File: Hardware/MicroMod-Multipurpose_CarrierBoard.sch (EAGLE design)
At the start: 85 parts, among them J11 microSD, J12 SPI, J14 I2C, J16 General GPIO, J17 I2C1, J3 JTAG, J5 UART, J6 MICROMOD-2222-C, J8 Dedicated, Q2 600mA/40V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

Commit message: Connect buzzer via MicroMod PWM0 via normally-connected trace
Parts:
- added BUZZER: JUMPER-COMBO_2_NC_TRACE, SparkFun-Jumpers:JUMPER-COMBO_2_NC_TRACE
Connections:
- net BUZZER: now also BUZZER.1
- net PWM0: now also BUZZER.2
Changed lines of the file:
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@@
 <part name="J17" library="SparkFun-Connectors" deviceset="I2C_STANDARD" device="_NO_SILK" value="I2C1"/>
 <part name="GND37" library="SparkFun-PowerSymbols" deviceset="GND" device=""/>
+<part name="BUZZER" library="SparkFun-Jumpers" deviceset="JUMPER-COMBO_2_NC_TRACE" device="" value=""/>
 </parts>
 <sheets>
@@
 <attribute name="VALUE" x="99.06" y="4.826" size="1.778" layer="96" align="top-center"/>
 </instance>
+<instance part="BUZZER" gate="JP1" x="386.08" y="134.62" smashed="yes" rot="R90">
+<attribute name="NAME" x="384.048" y="128.27" size="1.778" layer="95" font="vector" rot="R90"/>
+<attribute name="VALUE" x="388.62" y="132.08" size="1.778" layer="96" font="vector" rot="R90" align="top-left"/>
+</instance>
 </instances>
 <busses>
@@
 <label x="33.02" y="78.74" size="1.27" layer="95" rot="R180" xref="yes"/>
 </segment>
+<segment>
+<pinref part="BUZZER" gate="JP1" pin="2"/>
+<wire x1="386.08" y1="139.7" x2="386.08" y2="142.24" width="0.1524" layer="91"/>
+<wire x1="386.08" y1="142.24" x2="388.62" y2="142.24" width="0.1524" layer="91"/>
+<label x="388.62" y="142.24" size="1.27" layer="95" xref="yes"/>
+</segment>
 </net>
 <net name="PWM1" class="0">
@@
 <label x="78.74" y="38.1" size="1.27" layer="95" rot="R180" xref="yes"/>
 <pinref part="J12" gate="G$1" pin="5"/>
-</segment>
-</net>
-<net name="BUZZER" class="0">
-<segment>
-<pinref part="R17" gate="G$1" pin="1"/>
-<wire x1="396.24" y1="121.92" x2="393.7" y2="121.92" width="0.1524" layer="91"/>
-<label x="393.7" y="121.92" size="1.27" layer="95" rot="R180" xref="yes"/>
 </segment>
 </net>
@@
 </segment>
 </net>
+<net name="BUZZER" class="0">
+<segment>
+<pinref part="BUZZER" gate="JP1" pin="1"/>
+<wire x1="386.08" y1="129.54" x2="386.08" y2="127" width="0.1524" layer="91"/>
+<pinref part="R17" gate="G$1" pin="1"/>
+<wire x1="386.08" y1="127" x2="386.08" y2="121.92" width="0.1524" layer="91"/>
+<wire x1="386.08" y1="121.92" x2="396.24" y2="121.92" width="0.1524" layer="91"/>
+<wire x1="386.08" y1="127" x2="388.62" y2="127" width="0.1524" layer="91"/>
+<junction x="386.08" y="127"/>
+<label x="388.62" y="127" size="1.27" layer="95" xref="yes"/>
+</segment>
+</net>

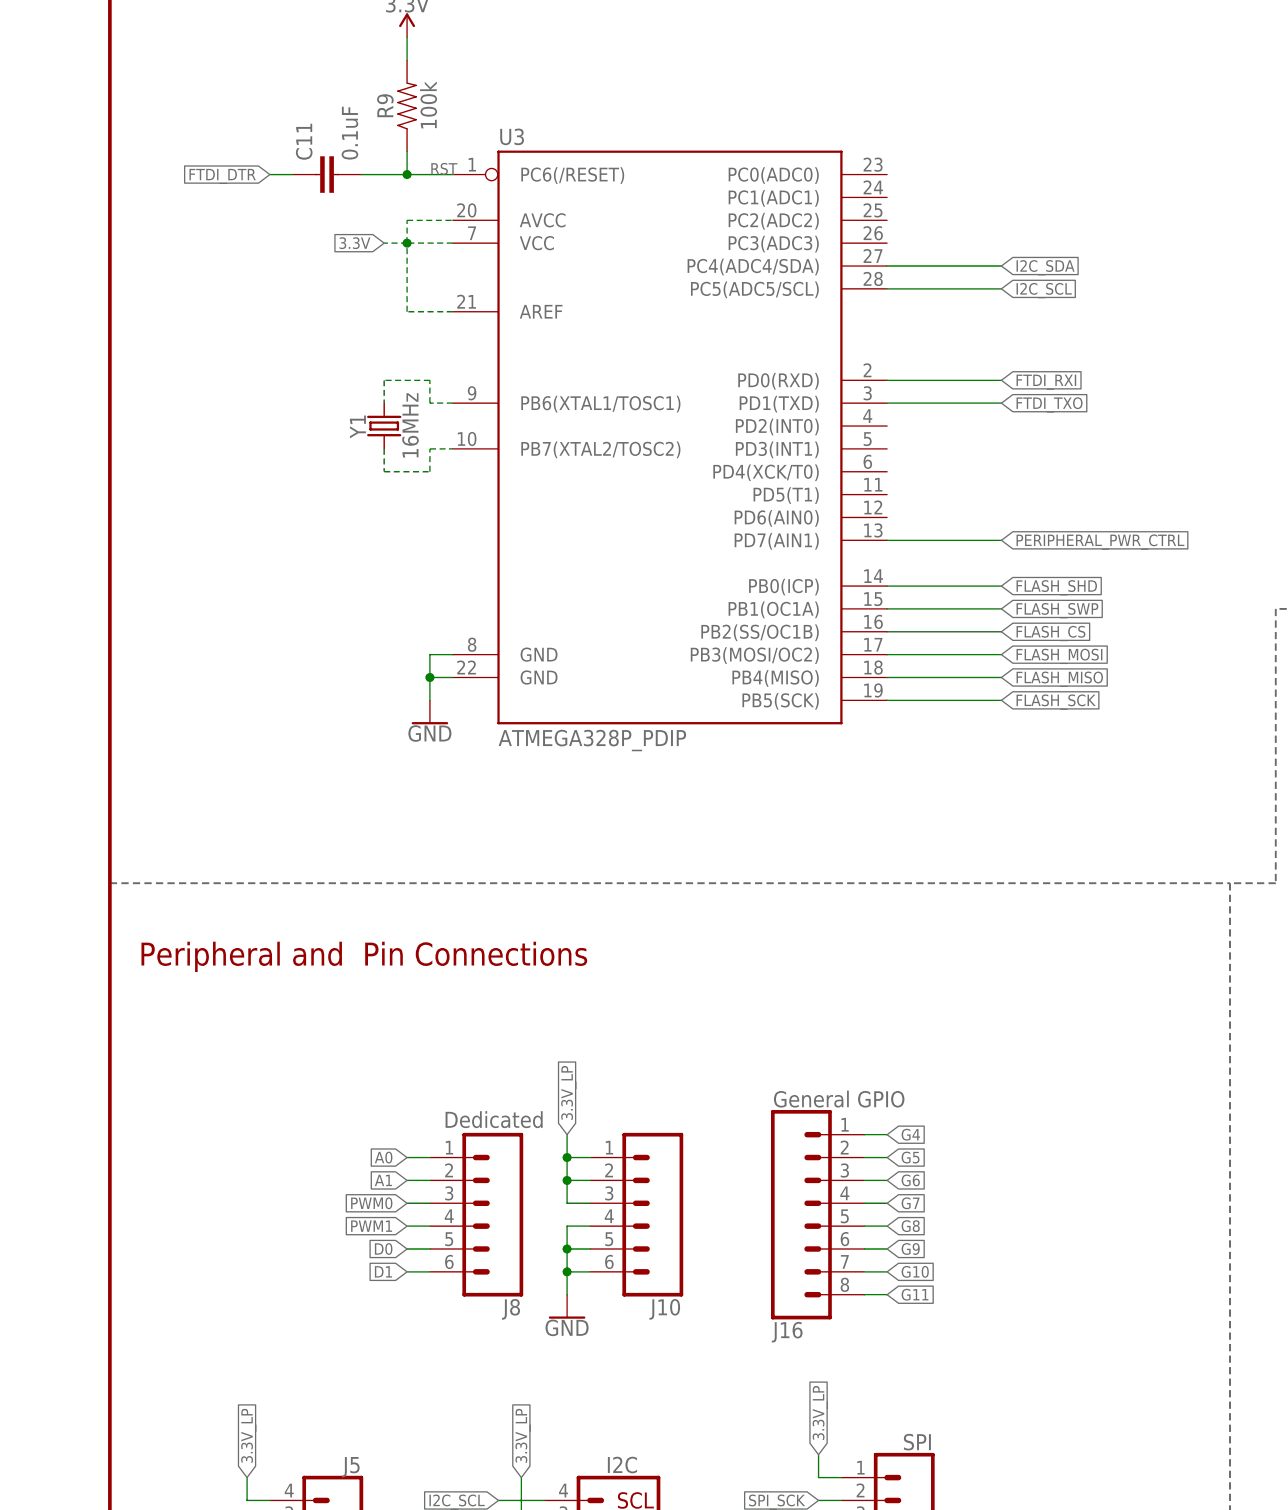
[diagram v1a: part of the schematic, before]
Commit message: Connect to I2C_SDA via via normally-connected trace & breakout ADC0-3
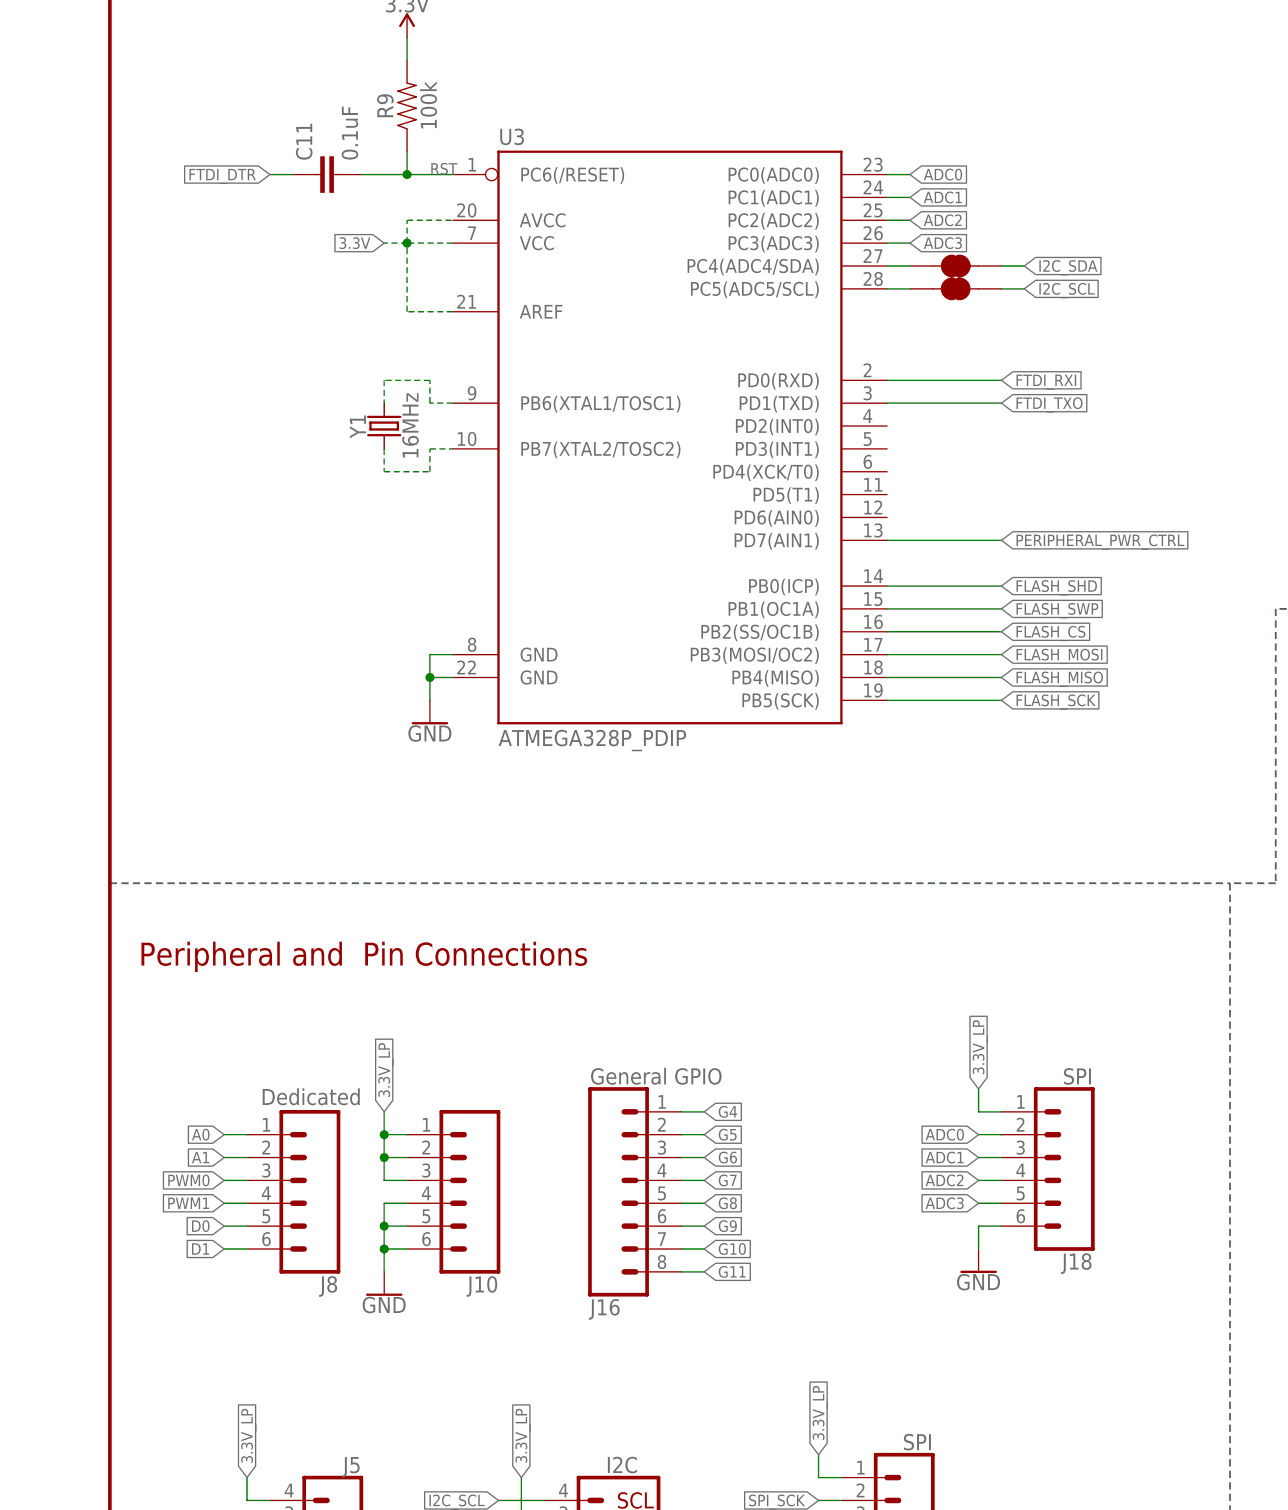
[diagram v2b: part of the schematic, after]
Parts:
- added I2C_SCL, I2C_SDA: JUMPER-COMBO_2_NC_TRACE, SparkFun-Jumpers:JUMPER-COMBO_2_NC_TRACE
- added J18: SPI, SparkFun-Connectors:CONN_06NO_SILK_NO_POP
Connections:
- new net ADC0: J18.2, U3.PC0(ADC0)
- new net ADC1: J18.3, U3.PC1(ADC1)
- new net ADC2: J18.4, U3.PC2(ADC2)
- new net ADC3: J18.5, U3.PC3(ADC3)
- new net N$17: I2C_SDA.1, U3.PC4(ADC4/SDA)
- new net N$18: I2C_SCL.2, U3.PC5(ADC5/SCL)
- net 3.3V_LP: now also J18.1
- net GND: now also J18.6
- net I2C_SCL: now also I2C_SCL.1; no longer U3.PC5(ADC5/SCL)
- net I2C_SDA: now also I2C_SDA.2; no longer U3.PC4(ADC4/SDA)
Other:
- moved on the sheet: J10, J16, J8

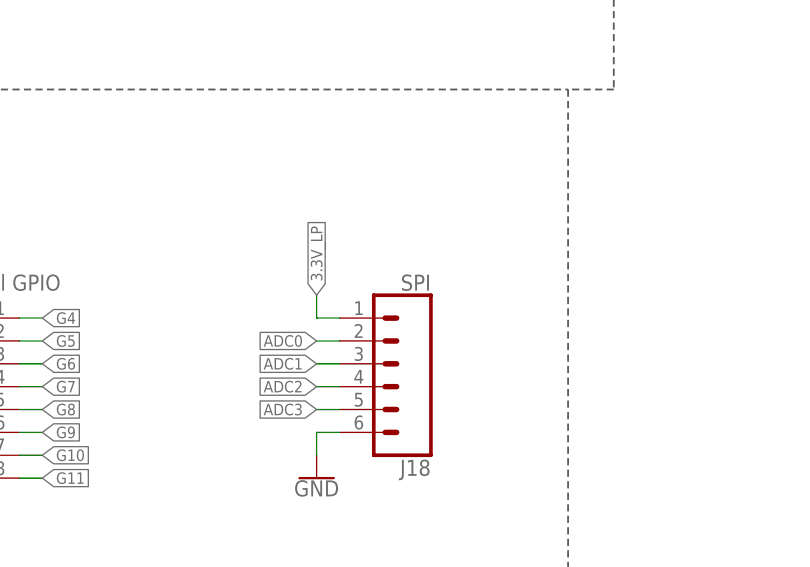
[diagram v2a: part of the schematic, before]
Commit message: FIX header name
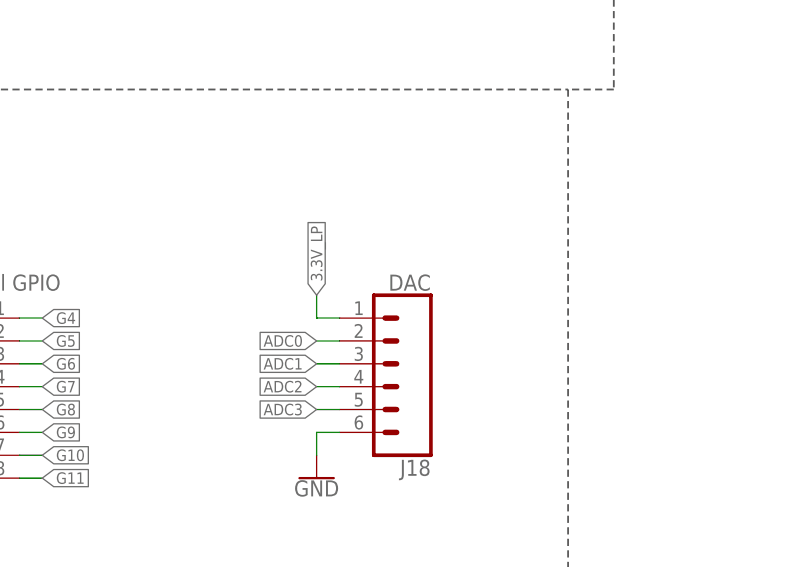
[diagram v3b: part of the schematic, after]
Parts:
- J18: value SPI -> DAC
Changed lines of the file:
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@@
 <part name="I2C_SDA" library="SparkFun-Jumpers" deviceset="JUMPER-COMBO_2_NC_TRACE" device="" value=""/>
 <part name="I2C_SCL" library="SparkFun-Jumpers" deviceset="JUMPER-COMBO_2_NC_TRACE" device="" value=""/>
-<part name="J18" library="SparkFun-Connectors" deviceset="CONN_06" device="NO_SILK_NO_POP" value="SPI"/>
+<part name="J18" library="SparkFun-Connectors" deviceset="CONN_06" device="NO_SILK_NO_POP" value="DAC"/>
 <part name="GND38" library="SparkFun-PowerSymbols" deviceset="GND" device=""/>
 </parts>

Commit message: Add 2.4" TFT and revise SPI connection
- Add notes for future changes
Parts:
- removed FLASH_VDD: JUMPER-SMT_2_NC_TRACE_SILK, SparkFun-Jumpers:JUMPER-SMT_2_NC_TRACE_SILK
- added C12: 0.1uF, SparkFun-Capacitors:0.1UF-0603-25V-(+80/-20%)
- added FRAME2: FRAME-LEDGER, SparkFun-Aesthetics:FRAME-LEDGER
- added J19: SPI1, SparkFun-Connectors:CONN_06NO_SILK_NO_POP
- added J20: 2.4" TFT, SparkFun-Displays:4DLCD-24-320X240
- added Q1: 1.1A/600mΩ, SparkFun-DiscreteSemi:MOSFET_PCH-SI2309DS
- added R18, R19, R20, R21, R22, R23: 100k, SparkFun-Resistors:100KOHM-0603-1/10W-1%
- added R24: 10, SparkFun-Resistors:10OHM-1206-1/4W-1%
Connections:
- removed net FLASH_CS: J15.6, J6.SPI_!CS1!/SDIO_DATA3, U1.CS, U3.PB2(SS/OC1B)
- removed net FLASH_MISO: J15.4, J6.SPI_SDI1/SDIO_DATA0, U1.MISO, U3.PB4(MISO)
- removed net FLASH_MOSI: J15.3, J6.SPI_SDO1/SDIO_CMD, U1.MOSI, U3.PB3(MOSI/OC2)
- removed net FLASH_SCK: J15.2, J6.SPI_SCK1/SDIO_CLK, U1.SCK, U3.PB5(SCK)
- removed net FLASH_VDD: C17.1, FLASH_VDD.1, J15.1, U1.VCC
- removed net G4: J16.1, J6.G4/BUS4
- removed net HEADER_!CS!: J12.5, J6.G0/BUS0
- removed net SD_!CS!: J11.DAT3/!CS!, J6.SPI_!CS!, R15.1
- removed net SPI_CIPO: J11.DAT0/SDO, J12.4, J6.SPI_SDI
- removed net SPI_COPI: J11.CMD/SDI, J12.3, J6.SPI_SDO
- new net !DISP_BL: Q1.G, R22.2, U3.PD5(T1)
- new net !DISP_CS: J20.CS, R21.1, U3.PD3(INT1)
- new net !DISP_RST: J20.RESET, R23.1, U3.PD4(XCK/T0)
- new net !FLASH_CS!: J15.6, J6.G1/BUS1, R18.1, U1.CS, U3.PB2(SS/OC1B)
- new net !SD_CS!: J11.DAT3/!CS!, J6.G0/BUS0, R15.1, U3.PD6(AIN0)
- new net !SPI_CS!: J12.5, J6.SPI_!CS!, R20.1
- new net !SPI_CS1!: J19.5, J6.SPI_!CS1!/SDIO_DATA3, R19.1
- new net DISP_D/!C: J20.D/C, U3.PD2(INT0)
- new net N$19: J20.LEDA, R24.1
- new net N$20: Q1.D, R24.2
- new net SPI_MISO: J12.4, J6.SPI_SDI
- new net SPI_MISO1: J11.DAT0/SDO, J15.4, J19.4, J20.SDO, J6.SPI_SDI1/SDIO_DATA0, U1.MISO, U3.PB4(MISO)
- new net SPI_MOSI: J12.3, J6.SPI_SDO
- new net SPI_MOSI1: J11.CMD/SDI, J15.3, J19.3, J20.SDI, J6.SPI_SDO1/SDIO_CMD, U1.MOSI, U3.PB3(MOSI/OC2)
- new net SPI_SCK1: J11.CLK/SCK, J15.2, J19.2, J20.SCK, J6.SPI_SCK1/SDIO_CLK, U1.SCK, U3.PB5(SCK)
- net 3.3V: now also C12.1, J20.VCC, Q1.S, R21.2, R23.2; no longer FLASH_VDD.2
- net 3.3V_LP: now also C17.1, J15.1, J19.1, R18.2, R19.2, R20.2, U1.VCC
- net GND: now also C12.2, J19.6, J20.GND, J20.LEDK, R22.1
- net PERIPHERAL_PWR_CTRL: now also J6.G4/BUS4; no longer J6.G1/BUS1
- net SPI_SCK: no longer J11.CLK/SCK
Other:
- note added: "2.4" TFT Screen"
- note added: "Optional considerations: - Remove Flash memory (as Processor modules have plenty). - Add 20/24bit DAC modules - Add quadrature encoder IC - Add thermocouple IC/thermocouple connector"

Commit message: Remove external Flash IC & connect inputs (buttons + joystick)
- Further refinement and cleaning up of connections
- 2.4" TFT VCC supply now tied to 3.3V_LP (via peripheral control) for
    low-quiescent current draw.
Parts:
- removed C17: 0.1uF, SparkFun-Capacitors:0.1UF-0402T-16V-10%
- removed J15: (no value), SparkFun-Connectors:CONN_08"
- removed R18: 100k, SparkFun-Resistors:100KOHM-0603-1/10W-1%
- removed U1: S25FL127SABMFI100, SparkFun-IC-Memory:SPI_FLASH-X25XXSMD1
- added S3, S4: MOMENTARY-SWITCH-SPST-SMD-5.2MM-TALL, SparkFun-Switches:MOMENTARY-SWITCH-SPST-SMD-5.2MM-TALL
- added S6: Joystick, SparkFun-Switches:JOYSTICK_MINI
- added TP1: TEST-POINT3, SparkFun-Connectors:TEST-POINT3
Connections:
- removed net !FLASH_CS!: J15.6, J6.G1/BUS1, R18.1, U1.CS, U3.PB2(SS/OC1B)
- removed net FLASH_SHD: J15.5, J6.G2/BUS2, U1.HOLD, U3.PB0(ICP)
- removed net FLASH_SWP: J15.7, J6.G3/BUS3, U1.WP, U3.PB1(OC1A)
- new net BTN_A: S3.2, U3.PD2(INT0)
- new net BTN_B: S4.2, U3.PD3(INT1)
- new net BTN_CENTER: S6.CENT, U3.PB0(ICP)
- new net BTN_DOWN: S6.DOWN, U3.PD5(T1)
- new net BTN_LEFT: S6.LEFT, U3.PD6(AIN0)
- new net BTN_RIGHT: S6.RIGHT, U3.PD7(AIN1)
- new net BTN_UP: S6.UP, U3.PD4(XCK/T0)
- net !DISP_BL: now also J6.G5/BUS5; no longer U3.PD5(T1)
- net !DISP_CS: now also J6.G2/BUS2; no longer U3.PD3(INT1)
- net !DISP_RST: now also J6.G4/BUS4; no longer U3.PD4(XCK/T0)
- net !SD_CS!: now also J6.G1/BUS1, U3.PB2(SS/OC1B); no longer J6.G0/BUS0, U3.PD6(AIN0)
- net 3.3V: no longer J20.VCC
- net 3.3V_LP: now also J20.VCC; no longer C17.1, J15.1, R18.2, U1.VCC
- net DISP_D/!C: now also J6.G3/BUS3; no longer U3.PD2(INT0)
- net G5: no longer J6.G5/BUS5
- net GND: now also S3.1, S4.1, S6.GND; no longer C17.2, J15.8, U1.GND
- net PERIPHERAL_PWR_CTRL: now also J6.G0/BUS0, U3.PB1(OC1A); no longer J6.G4/BUS4, U3.PD7(AIN1)
- net SPI_MISO1: no longer J15.4, U1.MISO
- net SPI_MOSI1: no longer J15.3, U1.MOSI
- net SPI_SCK1: no longer J15.2, U1.SCK
- net SWDCK: now also TP1.1
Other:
- note added: "Input Buttons"
- note added: "JTAG"
- note added: "Optional considerations: - Add 20/24bit DAC modules - Add quadrature encoder IC - Add thermocouple IC/thermocouple connector"
- note added: "TBD"
- note added: "pending"
- note removed: "128Mbit SPI Flash Memory"
- note removed: "Flash SPI Breakout"
- note removed: "Optional considerations: - Remove Flash memory (as Processor modules have plenty). - Add 20/24bit DAC modules - Add quadrature encoder IC - Add thermocouple IC/thermocouple connector"
- note removed: "SWO"
- note removed: "https://export.farnell.com/cypress-semiconductor/s25fl127sabmfi100/flash-memory-128mbit-soic-8/dp/2767980"
- moved on the sheet: C11, H5, J10, J12, J13, J14, J16, J17, J18, J19, J3, J5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

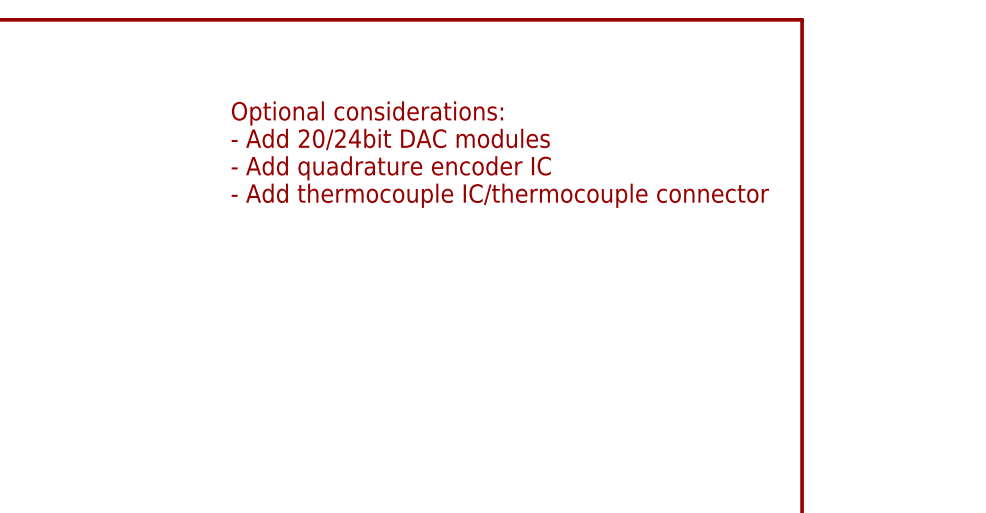
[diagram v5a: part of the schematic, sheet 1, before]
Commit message: Update notes for optional changes
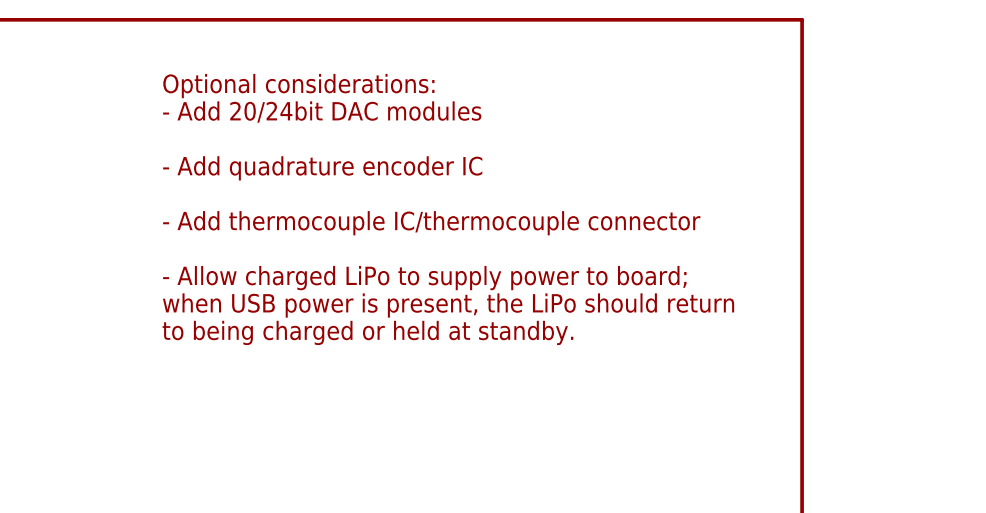
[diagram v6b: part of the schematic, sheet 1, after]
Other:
- note added: "Optional considerations: - Add 20/24bit DAC modules - Add quadrature encoder IC - Add thermocouple IC/thermocouple connector - Allow charged LiPo to supply power to board; when USB power is present, the LiPo should return to being charged or held at standby."
- note removed: "Optional considerations: - Add 20/24bit DAC modules - Add quadrature encoder IC - Add thermocouple IC/thermocouple connector"
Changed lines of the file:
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@@
 <wire x1="368.3" y1="106.68" x2="370.84" y2="106.68" width="0.2032" layer="97" style="longdash"/>
 <wire x1="370.84" y1="106.68" x2="370.84" y2="35.56" width="0.2032" layer="97" style="longdash"/>
-<text x="368.3" y="259.08" size="2.032" layer="94">Optional considerations:
+<text x="360.68" y="243.84" size="2.032" layer="94">Optional considerations:
 - Add 20/24bit DAC modules
 - Add quadrature encoder IC
 - Add thermocouple IC/thermocouple connector
-</text>
+- Allow charged LiPo to supply power to board;
+when USB power is present, the LiPo should return
+to being charged or held at standby.</text>
 <wire x1="137.16" y1="144.78" x2="132.08" y2="144.78" width="0.2032" layer="97" style="longdash"/>
 <wire x1="132.08" y1="144.78" x2="132.08" y2="124.46" width="0.2032" layer="97" style="longdash"/>
